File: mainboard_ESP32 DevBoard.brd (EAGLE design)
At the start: 54.9 x 106.7 mm, 43 parts, among them IC1 OP-AMP-2-LONG, IC2 OP-AMP-2-LONG, IC3 74HC08N, K1 AQH213, X1 JST-XH-02-PIN-LONG-PAD, X2 JST-XH-04-PIN-LONG-PAD, X3 1751248, X4 1751248, X5 JST-XH-04-PIN-LONG-PAD

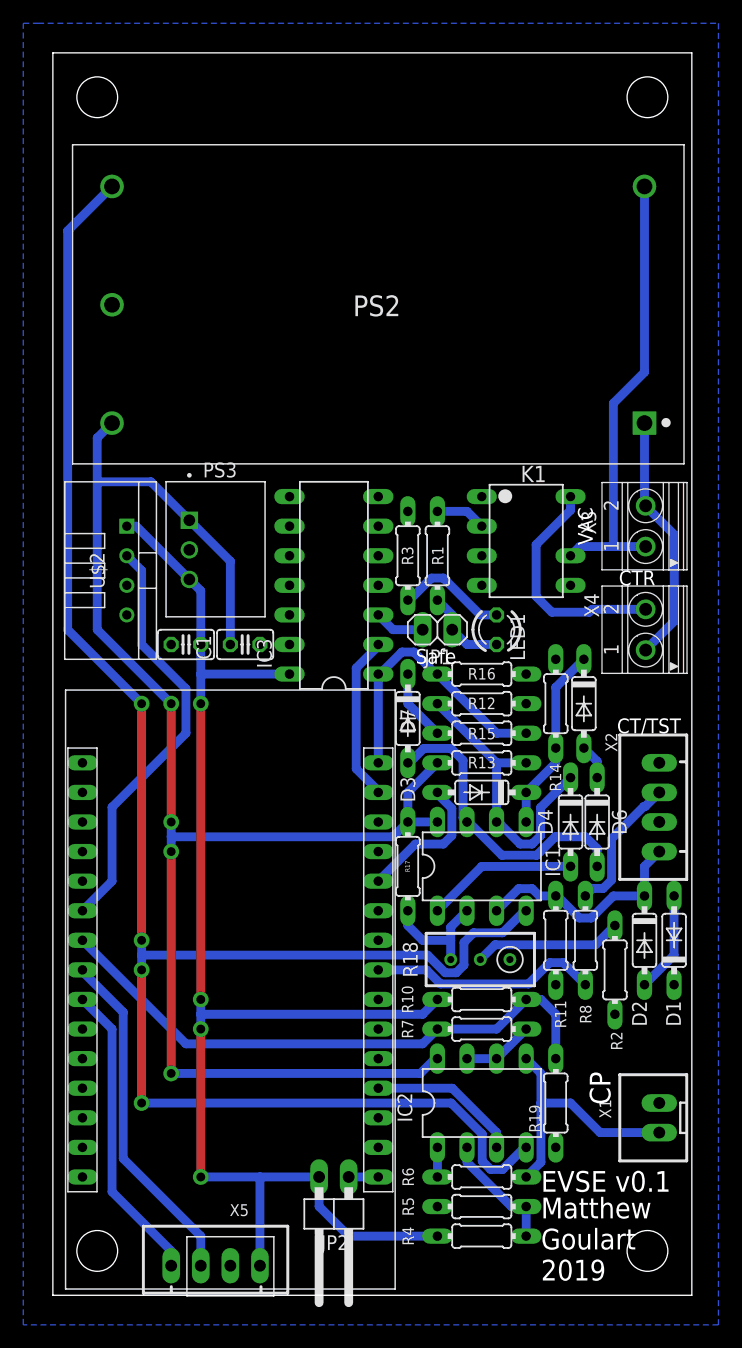
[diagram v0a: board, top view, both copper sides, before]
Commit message: Switched to +-12v, tweaked some R values to fit new psu. Also swapped CP opamp for an r2r one
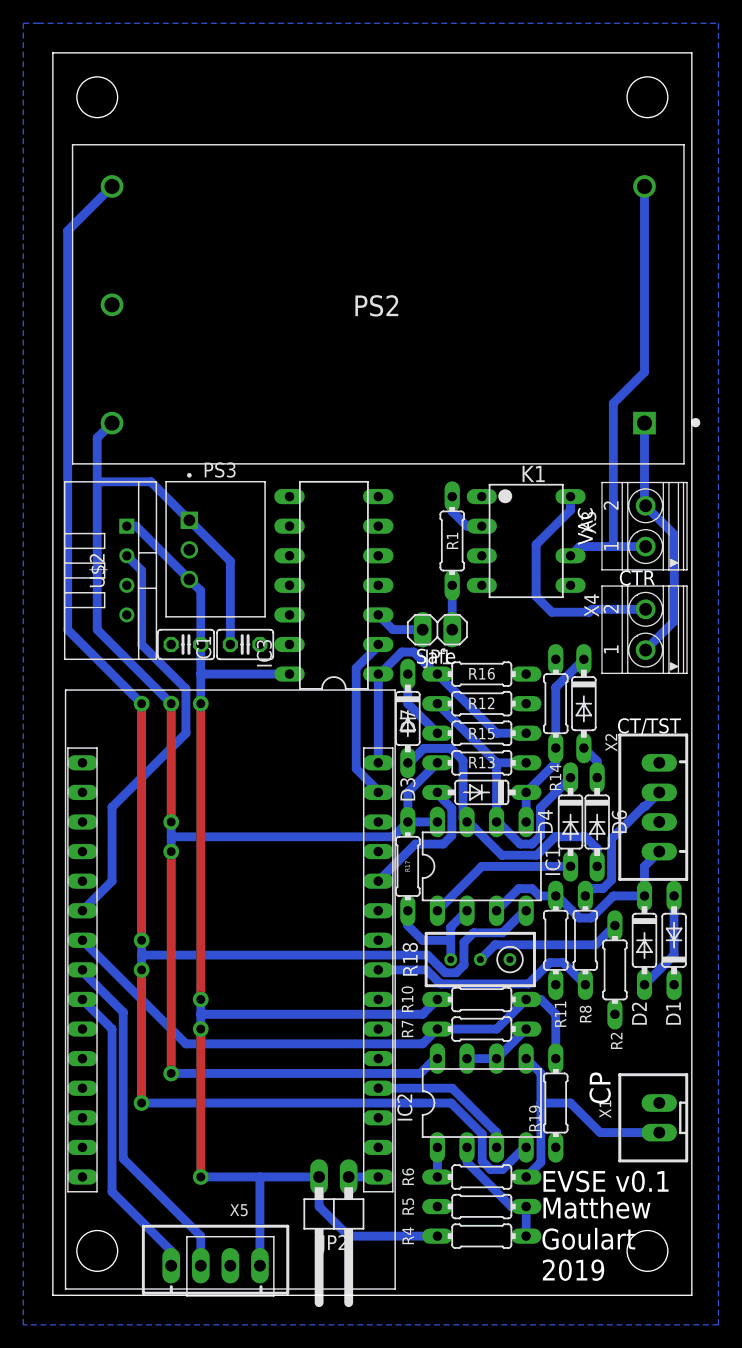
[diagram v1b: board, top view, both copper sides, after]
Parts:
- removed LED1: (no value), led:LED3MM
- removed R3: 130, Passive:0204/7-L
- PS2: value RAC10-15DK/277 -> RAC20-12DK; device RAC10-15DK_277:CONV_RAC10-15DK/277 -> RAC20-12DK:CONV_RAC20-12DK
- R1: value 330 -> 160
- R12: value 1.5K -> 2K
- R15: value 100K -> 10K
- R16: value 38.3K -> 3.9K
- R2: value 430 -> 560
- moved R1 1.80 mm to (34.3, 64.8)
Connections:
- net +15V renamed +12V
- net -15V renamed -12V
- removed net N$8: LED1.K, R3.1
- net GND: no longer K1.1, K1.4, R3.2
- net N$3: no longer LED1.A
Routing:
- net N$8: track 9.71 -> 0.00 mm
- net N$3: track 7.40 -> 3.81 mm

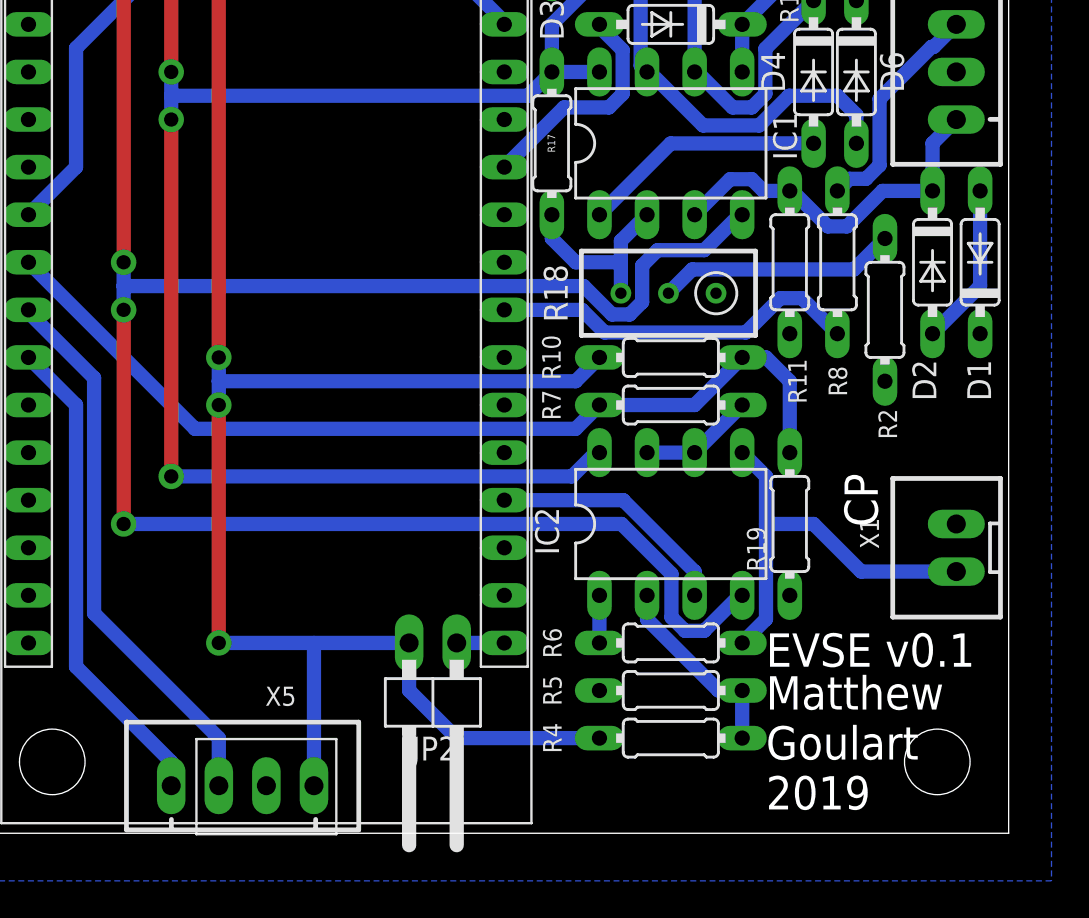
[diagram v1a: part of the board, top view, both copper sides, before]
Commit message: Added DG419 in place of op amp.
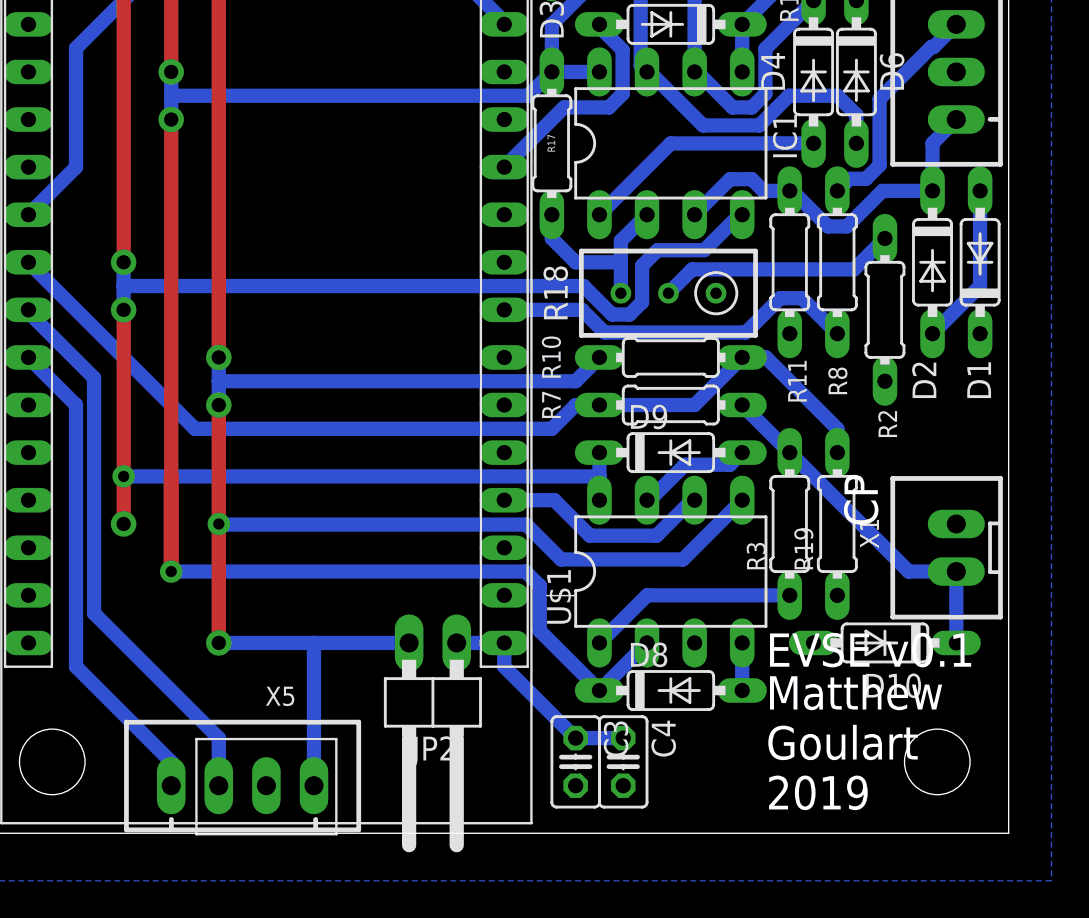
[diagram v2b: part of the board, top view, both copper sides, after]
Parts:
- removed IC2: OP-AMP-2-LONG, Op Amp:DIL08-LONG
- removed R4, R5: 100K, Passive:0204/7-L
- removed R6: 910, Passive:0204/7-L
- added C3: 0.1uF, rcl:C025-025X050
- added C4: 10uF, rcl:C025-025X050
- added D10: TVS 12.1V, Passive:DO35-7
- added D8, D9: 1N4148DO35-7, diode:DO35-7
- added R3: 910, Passive:0204/7-L
- added U$1: DG419DJ-L, Analog Switches:DIL08-LONG
- moved R19 2.54 mm to (45.7, 16.5)
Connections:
- removed net N$16: IC2.1, R6.1
- removed net N$17: IC2.6, IC2.7, R7.1
- new net N$11: D8.A, U$1.4
- new net N$8: R3.1, U$1.1
- net +12V: now also D8.C, U$1.2; no longer IC2.8
- net +3V3: now also U$1.5; no longer R4.2
- net -12V: now also D9.C, U$1.8; no longer IC2.4
- net CP: now also D10.C, R3.2, R7.1; no longer IC2.5, R6.2
- net CP_PWM: now also U$1.6; no longer IC2.3
- net GND: now also C3.2, C4.2, D10.A, U$1.3; no longer R5.1
- net N$10: now also C3.1, C4.1
- net N$15: now also D9.A, U$1.7; no longer IC2.2, R4.1, R5.2
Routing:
- net +3V3: track 119.0 -> 135.3 mm, vias 4 -> 5
- net +12V: track 133.3 -> 145.5 mm
- net N$8: track 0.00 -> 11.2 mm
- net -12V: track 157.4 -> 147.8 mm, vias 4 -> 5
- net N$10: track 2.54 -> 11.7 mm
- net N$17: track 6.13 -> 0.00 mm
- net N$15: track 10.5 -> 6.13 mm
- net CP: track 22.4 -> 18.9 mm
- net N$11: track 0.00 -> 2.54 mm
- net N$16: track 2.54 -> 0.00 mm
- net CP_PWM: track 13.0 -> 11.7 mm
- net CP_READ: track 50.2 -> 51.3 mm

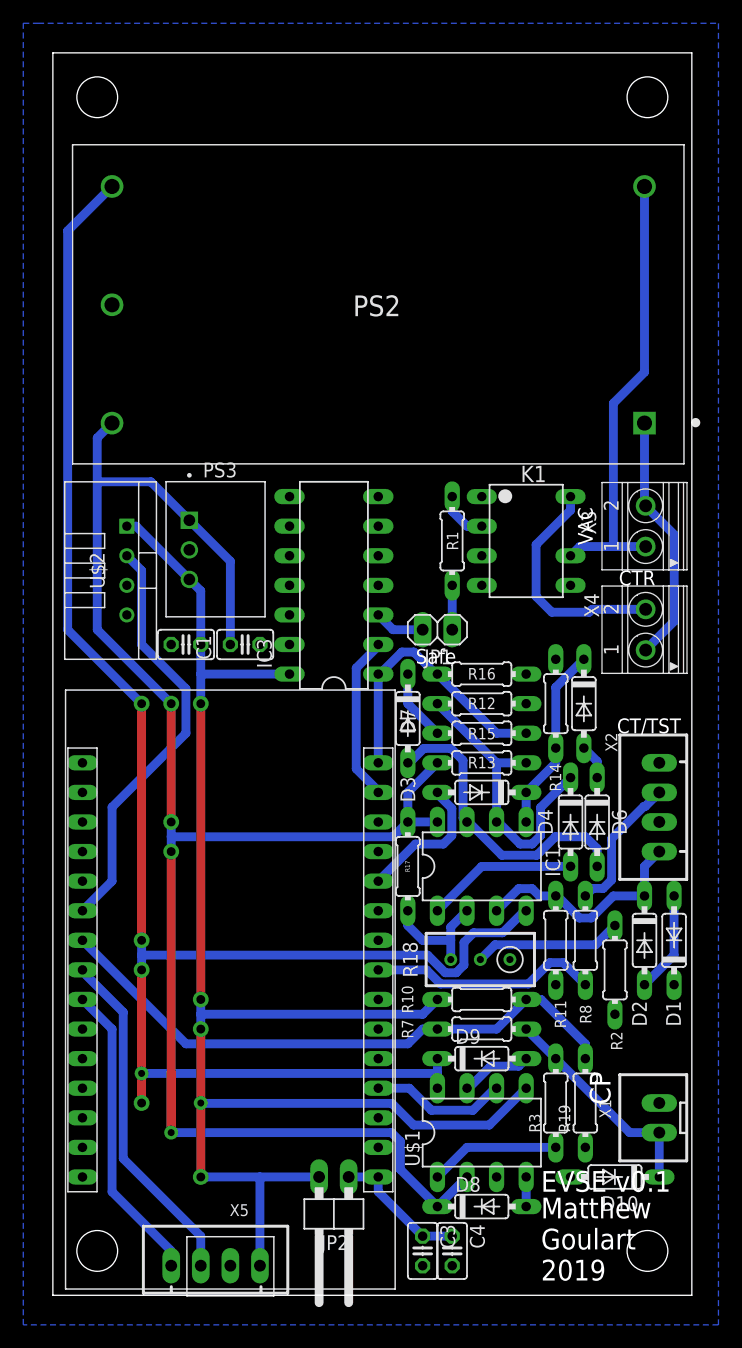
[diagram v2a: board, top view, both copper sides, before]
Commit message: Added optos for sensing L and N (l1/l2)
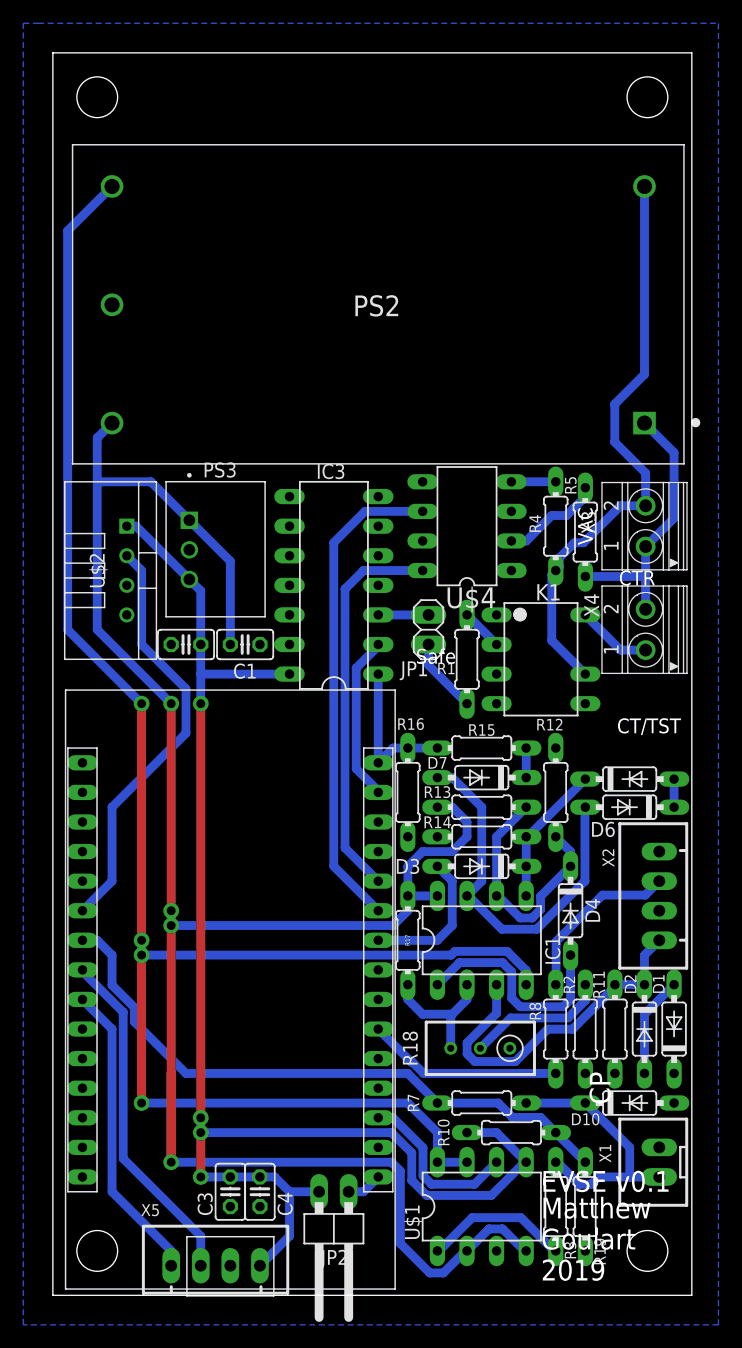
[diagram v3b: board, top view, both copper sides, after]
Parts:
- removed D8, D9: 1N4148DO35-7, diode:DO35-7
- added R4, R5: 750, Passive:0204/7-L
- added U$4: OPTOCOUPLER-2, optocouplers:DIL8
- moved C3 17.3 mm to (15.2, 8.89)
- moved C4 17.3 mm to (17.8, 8.89)
- moved R14 13.1 mm to (36.8, 39.4), turned to 0 degrees
- moved R16 12.0 mm to (30.5, 43.2), turned to 90 degrees
- moved R10 11.7 mm to (39.4, 14.0)
- moved K1 10.2 mm to (41.9, 54.6)
- moved R1 10.2 mm to (35.6, 54.6)
- moved R12 9.92 mm to (43.2, 43.2), turned to 270 degrees
- moved R11 9.16 mm to (48.3, 22.9)
- moved R19 8.89 mm to (45.7, 7.62)
- moved R3 8.89 mm to (43.2, 7.62)
- moved D7 8.13 mm to (36.8, 44.5), turned to 180 degrees
- moved R8 8.03 mm to (43.2, 22.9)
- moved D1 7.62 mm to (53.3, 22.9)
- moved D2 7.62 mm to (50.8, 22.9)
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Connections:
- removed net N$15: D9.A, U$1.7
- new net N$16: R5.1, U$4.2
- new net N$17: R4.1, U$4.4
- new net VACL_SENS: U$3.GPIO19, U$4.6
- new net VACN_SENS: U$3.GPIO21, U$4.8
- net +12V: now also U$1.4; no longer D8.C
- net +3V3: now also C3.1, C4.1
- net -12V: now also U$1.7; no longer D9.C
- net CP_PWM: now also U$3.GPIO15; no longer U$3.GPIO2
- net ENER_COIL: now also X4.1; no longer X4.2
- net GFI_SET: now also U$3.GPIO18; no longer U$3.GPIO21
- net GFI_TST_SIG: now also U$3.GPIO16; no longer U$3.GPIO5
- net GND: now also U$4.1, U$4.3, U$4.5, U$4.7
- net N$10: no longer C3.1, C4.1
- net N$11: now also K1.5; no longer D8.A, U$1.4
- net VACL: now also R4.2, X3.2; no longer X3.1
- net VACN: now also R5.2, X3.1, X4.2; no longer X3.2, X4.1
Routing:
- net VACL_SENS: track 0.00 -> 41.9 mm
- net VACN_SENS: track 0.00 -> 33.6 mm
- net +12V: track 145.5 -> 167.4 mm
- net ENER_COIL: track 19.9 -> 6.43 mm
- net +3V3: track 135.3 -> 123.6 mm, vias 5 -> 4
- net VACL: track 38.9 -> 50.3 mm
- net GFI_INT: track 24.0 -> 13.2 mm
- net CT: track 19.6 -> 29.7 mm
- net N$16: track 0.00 -> 8.70 mm
- net N$10: track 11.7 -> 3.07 mm
- net N$4: track 26.1 -> 32.4 mm
- net N$9: track 13.0 -> 19.2 mm
- net N$15: track 6.13 -> 0.00 mm
- net N$14: track 25.7 -> 21.4 mm
- net CP: track 18.9 -> 22.9 mm
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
